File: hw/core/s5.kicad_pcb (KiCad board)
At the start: 4 copper layers, 138.7 x 100 mm, 274 parts, among them J1 MSTB2,5/3-GF-5,08_1776511, J10 SWD_2x3, J11 MC1,5/5-GF-3,5_1843826, J12 USB-C_2171820001, J2 LPJG0926HENL, J3 LPJG0926HENL, J4 LPJG0926HENL, J5 LPJG0926HENL, J6 LPJG0926HENL, J7 Conn_01x03, J8 microSD, K1 HFD23-024-1ZS, Q1 NMOS, Q2 NMOS, Q3 NMOS, Q4 NMOS, Q5 NMOS, Q50 BSP315P, Q60 2N7002, SW2 SW_Push, U1 KSZ9477S, U10 TPS3823, U11 TLV62569, U12 AP2112K-1.8, U13 TPS23861, U14 LM5122, U15 DS18B20, U16 DS18B20, U17 SHT40-AD1B, U18 TPS7B6933QDCYRQ1, U19 STM32G071CBTx, U2 AMS1117-3.3, U20 TPS7B6933QDCYRQ1, U21 EL357N, U3 AP2112K-2.5, U4 AP2112K-1.2, U6 TPS54560, U7 T113-S3, U8 W25N02JWZEIF, U9 TPS23861, Y1 25MHz, Y2 24MHz, Y3 32.768kHz

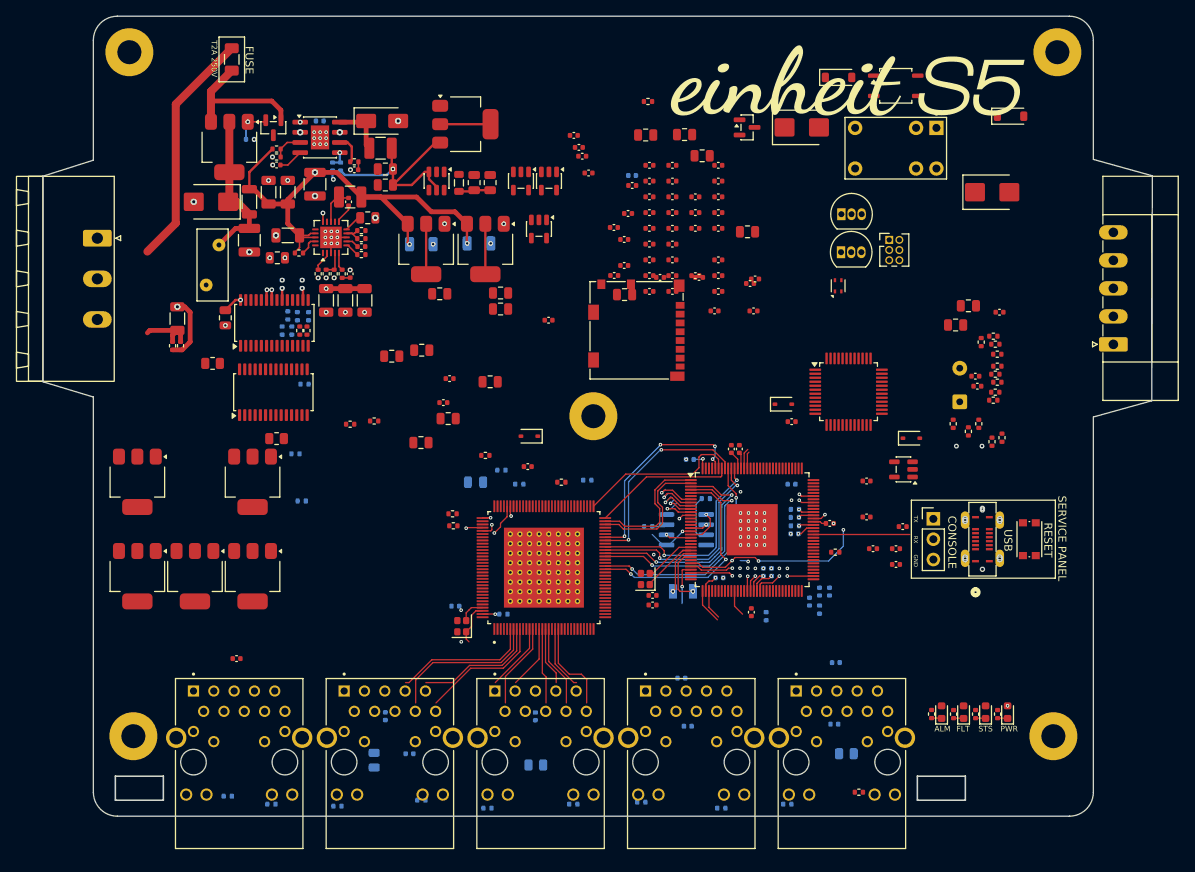
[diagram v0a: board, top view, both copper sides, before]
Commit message: s5: digital/power split, Mini-Fit interconnect, front-panel light guide
Land the board split and everything that followed from it:

- Move all switching (input protection, LM5122 boost, TPS54560 buck,
  3V3 LDO) to the power board; the core board receives finished rails.
- Board-to-board interconnect reduced to 8 pins: VBUS x2 + GND x2 +
  VIN_24V + VDD_5V + VDD_3V3 + MAIN_EN. Core J9 = Molex Mini-Fit Jr
  5569-08A1 2x4 right-angle header (serviceable, unplugs); power J2 =
  8-hole solder field (16AWG stripped ends, 1.7mm drill). Mate is an
  off-the-shelf Mini-Fit Versa 16AWG/9A cable assembly. Pin->net maps
  verified identical between the two boards.
- Front-panel status: Mentor 1278.1004 4-way bargraph light guide with
  Osram Mini TOPLED LEDs (green/yellow/orange/red), driven from the
  STM32 supervisor with PWM breathing; frees T113 PB7/PE4.
- PE: power-board input earth bonded to 4x M3_PE chassis mounting
  holes; the single GND<->PE bond stays on the core board.
- New footprints (light guide, Osram LED, 8-way solder field),
  per-board fp-lib-tables, and local vendor-3d models (${KIPRJMOD}).
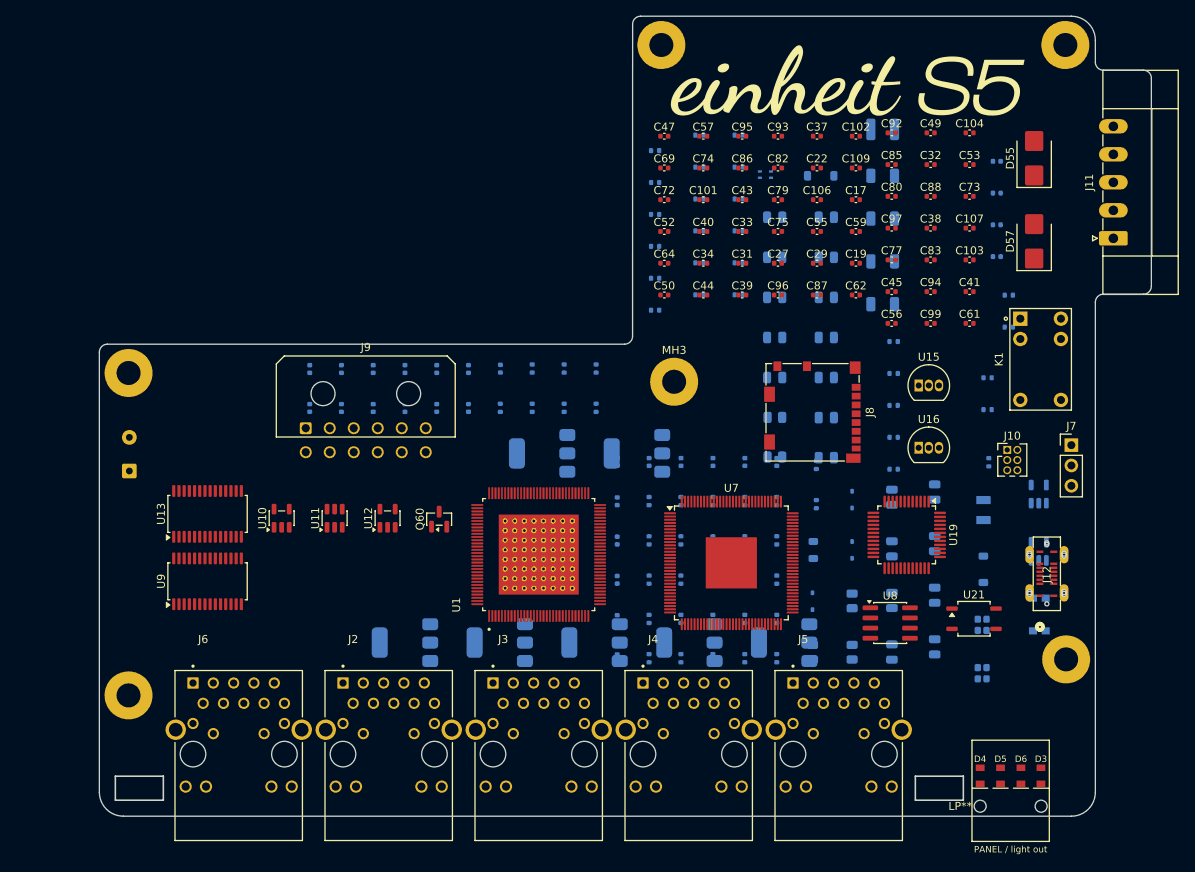
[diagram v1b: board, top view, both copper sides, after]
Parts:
- removed C111, C112, C114, C116, C117, C118, C119, C121, C122, C123, C124: 100nF, Capacitor_SMD:C_0402_1005Metric
- removed C113, C115: 10uF, Capacitor_SMD:C_0805_2012Metric
- removed C120: 4.7uF, Capacitor_SMD:C_0805_2012Metric
- removed C125: 4.7nF, Capacitor_SMD:C_1206_3216Metric
- removed D1: SS54, Diode_SMD:D_SMA
- removed D50: SMBJ30A, Diode_SMD:D_SMB
- removed D51: BZX84C12, Package_TO_SOT_SMD:SOT-23
- removed F1: Fuse_2A_TL, Fuse:Fuse_1206_3216Metric
- removed FB1: BLM31PG601SN1, Inductor_SMD:L_1206_3216Metric
- removed J1: MSTB2,5/3-GF-5,08_1776511, Connector_Phoenix_MSTB:PhoenixContact_MSTB_2,5_3-GF-5,08_1x03_P5.08mm_Horizontal_ThreadedFlange
- removed L2: 33uH, Inductor_SMD:L_1210_3225Metric
- removed L3: 1uH, Inductor_SMD:L_0805_2012Metric
- removed the MH1 at (90.5, 144.0)
- removed the MH3 at (206.0, 58.5)
- removed the MH4 at (148.0, 104.0)
- removed the MH4 at (205.5, 144.0)
- removed Q50: BSP315P, Package_TO_SOT_SMD:SOT-223-3_TabPin2
- removed R68, R69, R70, R78: 10k, Resistor_SMD:R_0402_1005Metric
- removed R71: 1k, Resistor_SMD:R_0402_1005Metric
- removed R72, R73, R74, R77: 4.7k, Resistor_SMD:R_0402_1005Metric
- removed R75: 270, Resistor_SMD:R_0402_1005Metric
- removed R76: 100k, Resistor_SMD:R_0402_1005Metric
- removed R79: 1M, Resistor_SMD:R_0402_1005Metric
- removed R80: 0R, Resistor_SMD:R_0402_1005Metric
- removed RV1: MOV_S14K30_DNP, Varistor:RV_Disc_D9mm_W3.9mm_P5mm
- removed U14: LM5122, Package_DFN_QFN:QFN-20-1EP_4x4mm_P0.5mm_EP2.7x2.7mm
- removed U2: AMS1117-3.3, Package_TO_SOT_SMD:SOT-223-3_TabPin2
- removed U6: TPS54560, Package_SO:SOIC-8-1EP_3.9x4.9mm_P1.27mm_EP2.29x3mm
- added J9: Conn_02x06, Connector_Molex:Molex_Micro-Fit_3.0_43045-1200_2x06_P3.00mm_Horizontal, F.Cu at (112.0, 105.5)
- added LP**: Mentor_1278.1004, Connector:Mentor_1278.1004_LightGuide, F.Cu at (200.2, 148.9)
- added MH1: MountingHole_M3_PE, MountingHole:MountingHole_3mm_Pad, F.Cu at (207.0, 57.6)
- added MH1: MountingHole_M3_PE, MountingHole:MountingHole_3mm_Pad, F.Cu at (156.5, 57.6)
- added MH3: MountingHole_M3_PE, MountingHole:MountingHole_3mm_Pad, F.Cu at (158.1, 99.7)
- added MH3: MountingHole_M3_PE, MountingHole:MountingHole_3mm_Pad, F.Cu at (89.9, 98.6)
- added MH4: MountingHole_M3_PE, MountingHole:MountingHole_3mm_Pad, F.Cu at (207.1, 134.4)
- C1, C35, C36, C42, C46, C48, C54, C58, C76, C84, C89, D2, D52, D53, D54, D56, Q1, Q2, Q3, Q4, Q5, R3, SW2, U17, U18, U20, U3, U4, Y1, Y2: moved to B.Cu
- C10, C8, C9: footprint Capacitor_SMD:C_1206_3216Metric -> Capacitor_SMD:C_0805_2012Metric; moved to B.Cu
- C100, C13: value 100nF -> 10uF; footprint Capacitor_SMD:C_0402_1005Metric -> Capacitor_SMD:C_0805_2012Metric
- C101, C69, C73, C74, C75, C77, C79, C88, C99, U8: moved to F.Cu
- C105: value 10uF -> 4.7uF; moved to B.Cu
- C106, C27, C29, C31: value 10uF -> 100nF; footprint Capacitor_SMD:C_0805_2012Metric -> Capacitor_SMD:C_0402_1005Metric
- C107: value 18pF -> 100nF
- C108: value 18pF -> 100nF; moved to B.Cu
- C11: value 22uF -> 10uF; footprint Capacitor_SMD:C_1206_3216Metric -> Capacitor_SMD:C_0805_2012Metric; moved to B.Cu
- C110: value 100nF -> 4.7nF; footprint Capacitor_SMD:C_0402_1005Metric -> Capacitor_SMD:C_1206_3216Metric; moved to B.Cu
- C12: value 22uF -> 10uF; footprint Capacitor_SMD:C_1206_3216Metric -> Capacitor_SMD:C_0805_2012Metric
- C14, C5, C51, C90, C91, C98: value 100nF -> 10uF; footprint Capacitor_SMD:C_0402_1005Metric -> Capacitor_SMD:C_0805_2012Metric; moved to B.Cu
- C15: value 15nF -> 10uF; footprint Capacitor_SMD:C_0402_1005Metric -> Capacitor_SMD:C_0805_2012Metric; moved to B.Cu
- C16: value 2.2uF -> 10uF; footprint Capacitor_SMD:C_1206_3216Metric -> Capacitor_SMD:C_0805_2012Metric; moved to B.Cu
- C17: value 2.2uF -> 100nF; footprint Capacitor_SMD:C_1206_3216Metric -> Capacitor_SMD:C_0402_1005Metric
- C18, C21: value 22uF -> 100nF; footprint Capacitor_SMD:C_0805_2012Metric -> Capacitor_SMD:C_0402_1005Metric; moved to B.Cu
- C19, C22: value 22uF -> 100nF; footprint Capacitor_SMD:C_0805_2012Metric -> Capacitor_SMD:C_0402_1005Metric
- C2: footprint Capacitor_SMD:C_1210_3225Metric -> Capacitor_SMD:C_1206_3216Metric; moved to B.Cu
- C20, C23, C24, C25, C26, C28, C30: value 10uF -> 100nF; footprint Capacitor_SMD:C_0805_2012Metric -> Capacitor_SMD:C_0402_1005Metric; moved to B.Cu
- C3: value 100uF -> 10uF
- C4: value 4.7uF -> 10uF; footprint Capacitor_SMD:C_0805_2012Metric -> Capacitor_SMD:C_1206_3216Metric; moved to B.Cu
- C49, C50: value 100nF -> 15pF
- C6: value 100nF -> 22uF; footprint Capacitor_SMD:C_0402_1005Metric -> Capacitor_SMD:C_0805_2012Metric; moved to B.Cu
- C63: footprint Capacitor_SMD:C_0402_1005Metric -> Capacitor_SMD:C_0805_2012Metric; moved to B.Cu
- C64: value 15pF -> 100nF
- C65: value 15pF -> 100nF; footprint Capacitor_SMD:C_0402_1005Metric -> Capacitor_SMD:C_0805_2012Metric
- C66: value 10uF -> 1uF; footprint Capacitor_SMD:C_0805_2012Metric -> Capacitor_SMD:C_0402_1005Metric
- C67: value 100nF -> 1uF
- C7: value 10nF -> 22uF; footprint Capacitor_SMD:C_0402_1005Metric -> Capacitor_SMD:C_0805_2012Metric; moved to B.Cu
- C78: footprint Capacitor_SMD:C_0805_2012Metric -> Capacitor_SMD:C_0402_1005Metric; moved to B.Cu
- C80: footprint Capacitor_SMD:C_0805_2012Metric -> Capacitor_SMD:C_0402_1005Metric
- C81: value 1uF -> 100nF; moved to B.Cu
- C82: value 1uF -> 100nF; moved to F.Cu
- C92: value 100nF -> 18pF; moved to F.Cu
- C93: value 100nF -> 18pF
- D3: value LED -> LG M676 green; footprint LED_SMD:LED_0603_1608Metric -> connectors:Osram_MiniTOPLED_LSM676
- D4: value LED -> LY M676 yellow; footprint LED_SMD:LED_0603_1608Metric -> connectors:Osram_MiniTOPLED_LSM676
- D5: value LED -> LO M676 orange; footprint LED_SMD:LED_0603_1608Metric -> connectors:Osram_MiniTOPLED_LSM676
- D6: value LED -> LS M676 red; footprint LED_SMD:LED_0603_1608Metric -> connectors:Osram_MiniTOPLED_LSM676
- J2, J3, J4, J5, J6: value LPJG0926HENL -> LINK-PP_LPJG0926HENL
- L1: value 10uH -> 1uH; footprint Inductor_SMD:L_1210_3225Metric -> Inductor_SMD:L_0805_2012Metric; moved to B.Cu
- R10, R9: value 100k -> 10k; moved to B.Cu
- R11: value 13k -> 10k; moved to B.Cu
- R12: value 24.9k -> 1k; moved to B.Cu
- R13: value 52.3k -> 150
- R14, R19: value 10k -> 150
- R15: value 50k -> 150; moved to B.Cu
- R16: value 100k -> 150; moved to B.Cu
- R17: value 6.04k -> 150
- R18: value 191 -> 150; moved to B.Cu
- R2: value 150k -> 50k; moved to B.Cu
- R20, R21: value 4.7k -> 150; moved to B.Cu
- R22: value 10k -> 150; moved to B.Cu
- R23: value 10k -> 47
- R24: value 10k -> 0.25; footprint Resistor_SMD:R_0402_1005Metric -> Resistor_SMD:R_0805_2012Metric
- R25: value 1k -> 22
- R26, R29, R32: value 150 -> 47
- R27, R30: value 150 -> 0.25; footprint Resistor_SMD:R_0402_1005Metric -> Resistor_SMD:R_0805_2012Metric
- R28, R31, R34, R35: value 150 -> 22
- R33: value 150 -> 0.25; footprint Resistor_SMD:R_0402_1005Metric -> Resistor_SMD:R_0805_2012Metric; moved to B.Cu
- R36, R39: value 47 -> 22
- R37: value 0.25 -> 47; footprint Resistor_SMD:R_0805_2012Metric -> Resistor_SMD:R_0402_1005Metric
- R38: value 22 -> 0.25; footprint Resistor_SMD:R_0402_1005Metric -> Resistor_SMD:R_0805_2012Metric
- R4: value 6.8k -> 6.04k; moved to B.Cu
- R40: value 0.25 -> 22; footprint Resistor_SMD:R_0805_2012Metric -> Resistor_SMD:R_0402_1005Metric
- R41: value 22 -> 4.7k
- R42: value 47 -> 4.7k
- R43: value 0.25 -> 240; footprint Resistor_SMD:R_0805_2012Metric -> Resistor_SMD:R_0402_1005Metric; moved to B.Cu
- R44: value 22 -> 10k
- R45: value 47 -> 10k; moved to B.Cu
- R46: value 0.25 -> 10k; footprint Resistor_SMD:R_0805_2012Metric -> Resistor_SMD:R_0402_1005Metric
- R47: value 22 -> 10k; moved to B.Cu
- R48, R49: value 22 -> 27
- R5: value 33k -> 191; moved to B.Cu
- R50: value 47 -> 5.1k
- R51: value 0.25 -> 5.1k; footprint Resistor_SMD:R_0805_2012Metric -> Resistor_SMD:R_0402_1005Metric; moved to B.Cu
- R52, R53: value 22 -> 270
- R54: value 4.7k -> 270
- R55: value 4.7k -> 10k
- R56: value 240 -> 10k
- R58: value 10k -> 1k
- R59, R60, R7, R8: value 10k -> 4.7k; moved to B.Cu
- R6: value 430k -> 10k; moved to B.Cu
- R61: value 27 -> 4.7k; moved to B.Cu
- R62: value 27 -> 270; moved to B.Cu
- R63: value 5.1k -> 100k; moved to B.Cu
- R64: value 5.1k -> 4.7k; moved to B.Cu
- R65: value 270 -> 10k; moved to B.Cu
- R66: value 270 -> 1M; moved to B.Cu
- R67: value 270 -> 0R; moved to B.Cu
- U11: value TLV62569 -> TLV62569PDDCR
- moved C76 109.4 mm to (198.4, 80.1), turned to 180 degrees
- moved TS1 104.2 mm to (90.0, 110.8)
- moved C68 103.2 mm to (198.4, 72.1), turned to 180 degrees
- moved C14 102.0 mm to (190.7, 132.8), turned to 90 degrees
- moved C78 97.7 mm to (198.4, 76.1), turned to 180 degrees
- moved R26 95.2 mm to (197.3, 103.2)
- moved R34 90.2 mm to (155.7, 78.8)
- moved R36 88.7 mm to (197.4, 109.8), turned to 90 degrees
- moved R15 83.9 mm to (199.9, 88.9), turned to 180 degrees
- moved C6 83.5 mm to (185.3, 133.5), turned to 90 degrees
- moved Q2 83.3 mm to (171.8, 132.3), turned to 180 degrees
- moved R2 81.4 mm to (199.9, 92.9), turned to 180 degrees
- moved MH2 80.4 mm to (89.9, 138.9)
- moved C1 80.4 mm to (184.2, 68.2), turned to 180 degrees
- moved C8 80.0 mm to (185.3, 127.0), turned to 90 degrees
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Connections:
- C1 pad 1: VIN_PROT -> VBUS_54V
- C10 pad 1: VBUS_54V -> VIN_24V
- C100 pad 1: VDD_CORE -> VDD_3V3_PSE
- C101 pad 1: VDD_1V8 -> VDD_3V3_PSE
- C102 pad 1: VDD_1V8 -> VDD_3V3_SB
- C103 pad 1: VDD_1V8 -> VDD_3V3_SB
- C104 pad 1: VDD_1V8 -> VDD_3V3_SB
- C105 pad 1: VDD_CORE -> VDD_3V3_SB
- C106 pad 1: VDD_3V3 -> MCU_NRST
- C107 pad 1: T113_DXIN -> VDD_3V3_SB
- C108 pad 1: T113_DXOUT -> VDD_3V3_SB
- C109 pad 1: SOC_RESET_N -> VDD_3V3_SB
- C11 pad 1: VIN_24V -> VDD_5V
- C110 pad 1: VDD_3V3 -> GND
- C110 pad 2: GND -> PE
- C12 pad 1: VIN_24V -> VDD_3V3
- C13 pad 1: BOOT -> VDD_2V5
- C13 pad 2: SW_NODE -> GND
- C14 pad 1: SS_TR -> VDD_1V2
- C15 pad 1: COMP_MID -> VDD_CORE
- C16 pad 1: VIN_24V -> VDD_1V8
- C17 pad 1: VIN_24V -> VDD_2V5
- C18 pad 1: VDD_5V -> VDD_2V5
- C19 pad 1: VDD_5V -> VDD_2V5
- C20 pad 1: VDD_5V -> VDD_2V5
- C21 pad 1: VDD_CORE -> VDD_2V5
- C22 pad 1: VDD_CORE -> VDD_2V5
- C23 pad 1: VDD_1V8 -> VDD_2V5
- C24 pad 1: VDD_1V8 -> VDD_2V5
- C25 pad 1: VIN_24V -> VDD_2V5
- C26 pad 1: VDD_5V -> VDD_1V2
- C27 pad 1: VDD_3V3 -> VDD_1V2
- C28 pad 1: VDD_2V5 -> VDD_1V2
- C3 pad 1: VIN_24V -> VDD_5V
- C30 pad 1: VDD_CORE -> VDD_1V2
- C31 pad 1: VDD_1V8 -> VDD_1V2
- C32 pad 1: VDD_2V5 -> VDD_1V2
- C33 pad 1: VDD_2V5 -> VDD_1V2
- C34 pad 1: VDD_2V5 -> VDD_1V2
- C35 pad 1: VDD_2V5 -> VDD_1V2
- C36 pad 1: VDD_2V5 -> VDD_1V2
- C37 pad 1: VDD_2V5 -> VDD_1V2
- C38 pad 1: VDD_2V5 -> VDD_1V2
- C39 pad 1: VDD_2V5 -> VDD_1V2
- C4 pad 1: BOOST_VCC -> VDD_3V3
- C40 pad 1: VDD_2V5 -> VDD_1V2
- C46 pad 1: VDD_1V2 -> VDD_3V3
- C47 pad 1: VDD_1V2 -> VDD_3V3
- C48 pad 1: VDD_1V2 -> VDD_3V3
- C49 pad 1: VDD_1V2 -> KSZ_XI
- C5 pad 1: BST_BOOST -> VDD_5V
- C5 pad 2: BOOST_SW -> GND
- C50 pad 1: VDD_1V2 -> KSZ_XO
- C51 pad 1: VDD_1V2 -> KSZ_RESET_N
- C52 pad 1: VDD_1V2 -> P1_CT1
- C53 pad 1: VDD_1V2 -> P1_CT2
- C54 pad 1: VDD_1V2 -> P2_CT1
- C55 pad 1: VDD_1V2 -> P2_CT2
- C56 pad 1: VDD_1V2 -> P3_CT1
- C57 pad 1: VDD_1V2 -> P3_CT2
- C58 pad 1: VDD_1V2 -> P4_CT1
- C59 pad 1: VDD_1V2 -> P4_CT2
- C6 pad 1: BOOST_SS -> VDD_CORE
- C60 pad 1: VDD_1V2 -> P5_CT1
- C61 pad 1: VDD_3V3 -> P5_CT2
- C62 pad 1: VDD_3V3 -> VDD_3V3_PSE
- C63 pad 1: VDD_3V3 -> VBUS_54V
- C64 pad 1: KSZ_XI -> VDD_3V3_PSE
- C65 pad 1: KSZ_XO -> VBUS_54V
- C66 pad 1: KSZ_RESET_N -> T113_LDOB_OUT
- C67 pad 1: P1_CT1 -> T113_LDOA_OUT
- C68 pad 1: P1_CT2 -> VDD_3V3
- C69 pad 1: P2_CT1 -> VDD_3V3
- C7 pad 1: BOOST_COMP_MID -> VDD_CORE
- C70 pad 1: P2_CT2 -> VDD_3V3
- C71 pad 1: P3_CT1 -> VDD_3V3
- C72 pad 1: P3_CT2 -> VDD_3V3
- C73 pad 1: P4_CT1 -> VDD_3V3
- C74 pad 1: P4_CT2 -> VDD_3V3
- C75 pad 1: P5_CT1 -> VDD_3V3
- C76 pad 1: P5_CT2 -> VDD_3V3
- C77 pad 1: VDD_3V3_PSE -> VDD_3V3
- C78 pad 1: VBUS_54V -> VDD_3V3
- C79 pad 1: VDD_3V3_PSE -> VDD_3V3
- C8 pad 1: VBUS_54V -> VDD_1V8
- C80 pad 1: VBUS_54V -> VDD_CORE
- C81 pad 1: T113_LDOA_OUT -> VDD_CORE
- C82 pad 1: T113_LDOB_OUT -> VDD_CORE
- C83 pad 1: VDD_3V3 -> VDD_CORE
- C84 pad 1: VDD_3V3 -> VDD_CORE
- C85 pad 1: VDD_3V3 -> VDD_CORE
- C86 pad 1: VDD_3V3 -> VDD_1V8
- C87 pad 1: VDD_3V3 -> VDD_1V8
- C88 pad 1: VDD_3V3 -> VDD_1V8
- C89 pad 1: VDD_3V3 -> VDD_1V8
- C9 pad 1: VBUS_54V -> VDD_1V8
- C90 pad 1: VDD_3V3 -> VDD_CORE
- C92 pad 1: VDD_3V3 -> T113_DXIN
- C93 pad 1: VDD_3V3 -> T113_DXOUT
- C94 pad 1: VDD_3V3 -> SOC_RESET_N
- C95 pad 1: VDD_CORE -> VDD_3V3
- C96 pad 1: VDD_CORE -> VDD_3V3
- C97 pad 1: VDD_CORE -> VDD_3V3_SB
- C98 pad 1: VDD_CORE -> VDD_3V3_SB
- C99 pad 1: VDD_CORE -> VDD_3V3_SB
- D3 pad 2: GND -> LED_PWR
- L1 pad 1: VIN_24V -> CORE_SW
- L1 pad 2: BOOST_SW -> VDD_CORE
- R1 pad 1: RP_GATE -> VDD_5V
- R1 pad 2: GND -> CORE_PG
- R10 pad 1: VIN_24V -> VDD_3V3
- R10 pad 2: MAIN_EN -> PME_N
- R11 pad 1: MAIN_EN -> VDD_3V3
- R11 pad 2: GND -> SYNCLKO
- R12 pad 1: COMP -> IBA
- R12 pad 2: COMP_MID -> GND
- R13 pad 1: VDD_5V -> VDD_3V3
- R13 pad 2: FB_5V -> P1_GRN_A
- R14 pad 1: FB_5V -> VDD_3V3
- R14 pad 2: GND -> P1_YEL_A
- R15 pad 1: VDD_CORE -> VDD_3V3
- R15 pad 2: FB_0V9 -> P2_GRN_A
- R16 pad 1: FB_0V9 -> VDD_3V3
- R16 pad 2: GND -> P2_YEL_A
- R17 pad 1: KSZ_ISET -> VDD_3V3
- R17 pad 2: GND -> P3_GRN_A
- R18 pad 1: KSZ_S_REXT -> VDD_3V3
- R18 pad 2: GND -> P3_YEL_A
- R19 pad 2: KSZ_RESET_N -> P4_GRN_A
- R2 pad 1: BOOST_RT -> VDD_CORE
- R2 pad 2: GND -> FB_0V9
- R20 pad 2: SPI_MOSI -> P4_YEL_A
- R21 pad 2: SPI_CS_N -> P5_GRN_A
- R22 pad 2: INTRP_N -> P5_YEL_A
- R23 pad 1: VDD_3V3 -> VBUS_54V
- R23 pad 2: PME_N -> U9_DRAIN16
- R24 pad 1: VDD_3V3 -> U9_SRC15
- R24 pad 2: SYNCLKO -> POE_VP_1
- R25 pad 1: IBA -> U9_SRC15
- R25 pad 2: GND -> U9_SEN15
- R26 pad 1: VDD_3V3 -> VBUS_54V
- R26 pad 2: P1_GRN_A -> U9_DRAIN20
- R27 pad 1: VDD_3V3 -> U9_SRC19
- R27 pad 2: P1_YEL_A -> POE_VP_2
- R28 pad 1: VDD_3V3 -> U9_SRC19
- R28 pad 2: P2_GRN_A -> U9_SEN19
- R29 pad 1: VDD_3V3 -> VBUS_54V
- R29 pad 2: P2_YEL_A -> U9_DRAIN9
- R3 pad 1: VIN_24V -> FB_0V9
- R3 pad 2: BOOST_UVLO -> GND
- R30 pad 1: VDD_3V3 -> U9_SRC8
- R30 pad 2: P3_GRN_A -> POE_VP_3
- R31 pad 1: VDD_3V3 -> U9_SRC8
- R31 pad 2: P3_YEL_A -> U9_SEN8
- R32 pad 1: VDD_3V3 -> VBUS_54V
- R32 pad 2: P4_GRN_A -> U9_DRAIN13
- R33 pad 1: VDD_3V3 -> U9_SRC12
- R33 pad 2: P4_YEL_A -> POE_VP_4
- R34 pad 1: VDD_3V3 -> U9_SRC12
- R34 pad 2: P5_GRN_A -> U9_SEN12
- R35 pad 1: VDD_3V3 -> U9_KSENSA
- R35 pad 2: P5_YEL_A -> GND
- R36 pad 1: VBUS_54V -> U9_KSENSB
- R36 pad 2: U9_DRAIN16 -> GND
- R37 pad 1: U9_SRC15 -> VBUS_54V
- R37 pad 2: POE_VP_1 -> U13_DRAIN16
- R38 pad 1: U9_SRC15 -> U13_SRC15
- R38 pad 2: U9_SEN15 -> POE_VP_5
- R39 pad 1: VBUS_54V -> U13_SRC15
- R39 pad 2: U9_DRAIN20 -> U13_SEN15
- R4 pad 1: BOOST_UVLO -> KSZ_ISET
- R40 pad 1: U9_SRC19 -> U13_KSENSA
- R40 pad 2: POE_VP_2 -> GND
- R41 pad 1: U9_SRC19 -> VDD_3V3
- R41 pad 2: U9_SEN19 -> PSE_I2C_SDA
- R42 pad 1: VBUS_54V -> VDD_3V3
- R42 pad 2: U9_DRAIN9 -> PSE_I2C_SCL
- R43 pad 1: U9_SRC8 -> T113_DZQ
- R43 pad 2: POE_VP_3 -> GND
- R44 pad 1: U9_SRC8 -> VDD_3V3
- R44 pad 2: U9_SEN8 -> SOC_RESET_N
- R45 pad 1: VBUS_54V -> VDD_3V3
- R45 pad 2: U9_DRAIN13 -> FLASH_WP
- R46 pad 1: U9_SRC12 -> VDD_3V3
- R46 pad 2: POE_VP_4 -> FLASH_HOLD
- R47 pad 1: U9_SRC12 -> VDD_3V3_SB
- R47 pad 2: U9_SEN12 -> STM_WD_RST
- R48 pad 1: U9_KSENSA -> USB_DP
- R48 pad 2: GND -> USB_CONN_DP
- R49 pad 1: U9_KSENSB -> USB_DM
- R49 pad 2: GND -> USB_CONN_DM
- R5 pad 1: BOOST_ILIM -> KSZ_S_REXT
- R50 pad 1: VBUS_54V -> USB_CC1
- R50 pad 2: U13_DRAIN16 -> GND
- R51 pad 1: U13_SRC15 -> USB_CC2
- R51 pad 2: POE_VP_5 -> GND
- R52 pad 1: U13_SRC15 -> VDD_3V3_SB
- R52 pad 2: U13_SEN15 -> LED_PWR_A
- R53 pad 1: U13_KSENSA -> VDD_3V3_SB
- R53 pad 2: GND -> LED_STA_A
- R54 pad 1: VDD_3V3 -> VDD_3V3_SB
- R54 pad 2: PSE_I2C_SDA -> LED_FAULT_A
- R55 pad 1: VDD_3V3 -> VDD_3V3_PSE
- R55 pad 2: PSE_I2C_SCL -> PSE_RESET_N
- R56 pad 1: T113_DZQ -> VDD_3V3_SB
- R56 pad 2: GND -> MCU_NRST
- R57 pad 1: VDD_3V3 -> MCU_SWCLK
- R57 pad 2: SOC_RESET_N -> GND
- R58 pad 1: VDD_3V3 -> MCU_BOOT0_CTL
- R58 pad 2: FLASH_WP -> MCU_SWCLK
- R59 pad 1: VDD_3V3 -> VDD_3V3_SB
- R59 pad 2: FLASH_HOLD -> SUP_1WIRE
- R6 pad 1: VBUS_54V -> VDD_3V3
- R6 pad 2: BOOST_FB -> KSZ_RESET_N
- R60 pad 2: STM_WD_RST -> SUP_I2C_SCL
- R61 pad 1: USB_DP -> VDD_3V3_SB
- R61 pad 2: USB_CONN_DP -> SUP_I2C_SDA
- R62 pad 1: USB_DM -> VDD_3V3_SB
- R62 pad 2: USB_CONN_DM -> LED_ALM_A
- R63 pad 1: USB_CC1 -> RELAY_GATE
- R64 pad 1: USB_CC2 -> DI_TERM_P
- R64 pad 2: GND -> DI_LED_A
- R65 pad 1: VDD_3V3 -> VDD_3V3_SB
- R65 pad 2: LED_PWR_A -> DI_SENSE
- R66 pad 1: VDD_3V3 -> GND
- R66 pad 2: LED_STA_A -> PE
- R67 pad 1: VDD_3V3 -> GND
- R67 pad 2: LED_FAULT_A -> PE
- R7 pad 1: BOOST_FB -> VDD_3V3
- R7 pad 2: GND -> SPI_MOSI
- R8 pad 1: BOOST_COMP -> VDD_3V3
- R8 pad 2: BOOST_COMP_MID -> SPI_CS_N
- R9 pad 1: VIN_24V -> VDD_3V3
- R9 pad 2: BOOST_PG -> INTRP_N
- U11 pad 1: CORE_SW -> VDD_5V
- U11 pad 3: VDD_5V -> CORE_SW
- U11 pad 4: FB_0V9 -> VDD_5V
- U11 pad 5: VDD_5V -> CORE_PG
- U11 pad 6: GND -> FB_0V9
- U19 pad 18: (no net) -> LED_PWR
- U19 pad 40: (no net) -> LED_STATUS
- U19 pad 41: (no net) -> LED_FAULT
- U7 pad 20: VDD_3V3 -> VDD_1V8
- U7 pad 26: VDD_3V3 -> VDD_1V8
- U7 pad 43: LED_FAULT -> (no net)
- U7 pad 46: VDD_3V3 -> VDD_CORE
- U7 pad 48: VDD_1V8 -> T113_LDOB_OUT
- U7 pad 49: VDD_1V8 -> T113_LDOB_OUT
- U7 pad 51: VDD_3V3 -> VDD_CORE
- U7 pad 79: LED_STATUS -> (no net)
- U7 pad 81: VDD_3V3 -> VDD_CORE
- U7 pad 89: VDD_3V3 -> VDD_1V8
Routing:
- net PE: track 421.8 -> 0.00 mm
- net VIN_24V: track 68.0 -> 0.00 mm, vias 4 -> 0
- net SPI_CS_N: track 52.6 -> 0.00 mm, vias 2 -> 0
- net SPI_MISO: track 31.5 -> 0.00 mm, vias 2 -> 0
- net VBUS_54V: track 30.1 -> 0.00 mm, vias 6 -> 0
- net VIN_RAW: track 29.8 -> 0.00 mm
- net VDD_3V3: track 29.1 -> 0.00 mm, vias 7 -> 0
- net RGMII_TXD3: track 28.7 -> 0.00 mm, vias 2 -> 0
- net RGMII_TXD2: track 28.6 -> 0.00 mm, vias 2 -> 0
- net RGMII_TX_CTL: track 28.2 -> 0.00 mm, vias 2 -> 0
- net RGMII_TX_CLK: track 28.1 -> 0.00 mm, vias 2 -> 0
- net VDD_5V: track 27.7 -> 0.00 mm, vias 1 -> 0
- net SPI_CLK: track 27.4 -> 0.00 mm, vias 2 -> 0
- net RGMII_TXD1: track 27.1 -> 0.00 mm, vias 2 -> 0
- net RGMII_TXD0: track 26.2 -> 0.00 mm, vias 2 -> 0
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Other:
- board size 138.7 x 100 mm -> 131.5 x 100 mm
- board text removed: "ALM"
- board text removed: "CONSOLE"
- board text removed: "FLT"
- board text removed: "FUSE"
- board text removed: "GND"
- board text removed: "PWR"
- board text removed: "RESET"
- board text removed: "RX"
- board text removed: "SERVICE PANEL"
- board text removed: "STS"
- board text removed: "T2A 250V"
- board text removed: "TX"
- board text removed: "USB"
